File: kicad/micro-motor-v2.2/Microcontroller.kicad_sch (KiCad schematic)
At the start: 20 parts, among them J301 USB, J302 UART, J303 SWD, U301 STM32G474CET6

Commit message: ready to order
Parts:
- R305, R306: now not fitted; now left out of the parts list
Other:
- title: Micro-Motor V2.1 -> Micro-Motor V2.2
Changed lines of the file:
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@@
   (paper "A3")
   (title_block
-    (title "Micro-Motor V2.1")
+    (title "Micro-Motor V2.2")
     (date "2021-07-31")
     (rev "1")
@@
   (symbol (lib_id "stm32:STM32G474C(B-C-E)Tx_u") (at 228.6 127 180) (unit 2)
     (in_bom yes) (on_board yes) (dnp no)
-    (property "Reference" "U301" (at 227.1268 117.9322 0)
-      (effects (font (size 1.27 1.27)))
-    )
-    (property "Value" "STM32G474CET6" (at 227.1268 120.2436 0)
-      (effects (font (size 1.27 1.27)))
-    )
-    (property "Footprint" "LQFP48" (at 227.1268 122.555 0)
+    (property "Reference" "U301" (at 227.33 102.87 0)
+      (effects (font (size 1.27 1.27)))
+    )
+    (property "Value" "STM32G474CET6" (at 227.33 105.41 0)
+      (effects (font (size 1.27 1.27)))
+    )
+    (property "Footprint" "LQFP48" (at 227.33 151.13 0)
       (effects (font (size 1.27 1.27) italic))
     )
@@
   (symbol (lib_id "stm32:STM32G474C(B-C-E)Tx_u") (at 246.38 58.42 180) (unit 1)
     (in_bom yes) (on_board yes) (dnp no)
-    (property "Reference" "U301" (at 246.1768 49.3522 0)
-      (effects (font (size 1.27 1.27)))
-    )
-    (property "Value" "STM32G474CET6" (at 246.1768 51.6636 0)
-      (effects (font (size 1.27 1.27)))
-    )
-    (property "Footprint" "Package_QFP:LQFP-48_7x7mm_P0.5mm" (at 246.1768 53.975 0)
+    (property "Reference" "U301" (at 246.38 33.02 0)
+      (effects (font (size 1.27 1.27)))
+    )
+    (property "Value" "STM32G474CET6" (at 246.38 35.56 0)
+      (effects (font (size 1.27 1.27)))
+    )
+    (property "Footprint" "Package_QFP:LQFP-48_7x7mm_P0.5mm" (at 246.38 83.82 0)
       (effects (font (size 1.27 1.27) italic))
     )
@@
       (effects (font (size 1.27 1.27)))
     )
-    (property "Value" "STM32G474CET6" (at 353.06 184.15 0)
+    (property "Value" "STM32G474CET6" (at 347.98 184.15 0)
       (effects (font (size 1.27 1.27)))
     )
@@
   (symbol (lib_id "stm32:STM32G474C(B-C-E)Tx_u") (at 340.36 170.18 180) (unit 6)
     (in_bom yes) (on_board yes) (dnp no)
-    (property "Reference" "U301" (at 346.202 169.1386 0)
+    (property "Reference" "U301" (at 354.33 168.91 0)
       (effects (font (size 1.27 1.27)) (justify right))
     )
-    (property "Value" "STM32G474CET6" (at 346.202 171.45 0)
+    (property "Value" "STM32G474CET6" (at 354.33 171.45 0)
       (effects (font (size 1.27 1.27)) (justify right))
     )
-    (property "Footprint" "Package_QFP:LQFP-48_7x7mm_P0.5mm" (at 346.202 173.7614 0)
+    (property "Footprint" "Package_QFP:LQFP-48_7x7mm_P0.5mm" (at 354.33 173.99 0)
       (effects (font (size 1.27 1.27) italic) (justify right))
     )
@@
       (effects (font (size 1.27 1.27)) (justify left))
     )
-    (property "Value" "1k" (at 221.488 238.633 0)
+    (property "Value" "1k" (at 219.71 238.76 90)
       (effects (font (size 1.27 1.27)) (justify left))
     )
@@
   )
   (symbol (lib_id "Device:R") (at 238.76 237.49 0) (unit 1)
-    (in_bom yes) (on_board yes) (dnp no)
+    (in_bom no) (on_board yes) (dnp yes)
     (property "Reference" "R305" (at 240.538 236.3216 0)
       (effects (font (size 1.27 1.27)) (justify left))
     )
-    (property "Value" "1k" (at 240.538 238.633 0)
+    (property "Value" "1k" (at 238.76 238.76 90)
       (effects (font (size 1.27 1.27)) (justify left))
     )
@@
   )
   (symbol (lib_id "Device:R") (at 256.54 237.49 0) (unit 1)
-    (in_bom yes) (on_board yes) (dnp no)
+    (in_bom no) (on_board yes) (dnp yes)
     (property "Reference" "R306" (at 258.318 236.3216 0)
       (effects (font (size 1.27 1.27)) (justify left))
     )
-    (property "Value" "1k" (at 258.318 238.633 0)
-      (effects (font (size 1.27 1.27)) (justify left))
-    )
+    (property "Value" "1k" (at 256.54 238.76 90)
+      (effects (font (size 1.27 1.27)) (justify left))
+    )

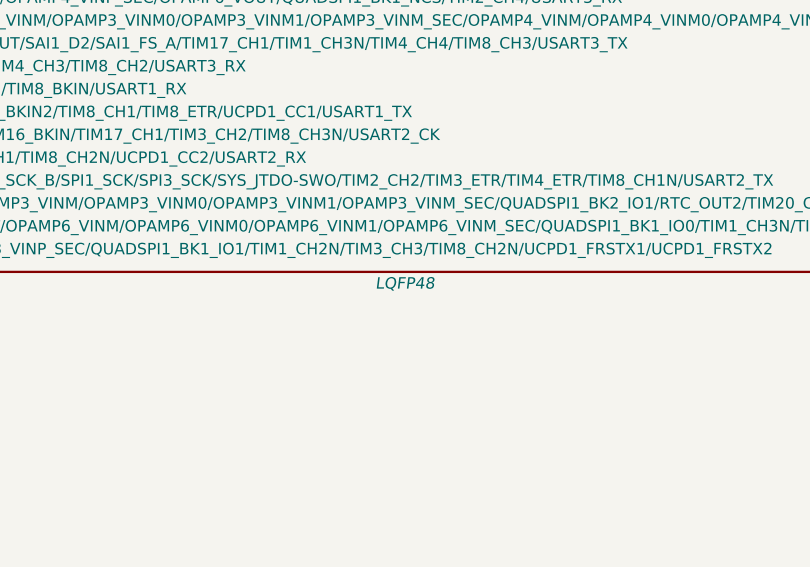
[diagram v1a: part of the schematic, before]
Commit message: [CI] Attempt to fix ERC
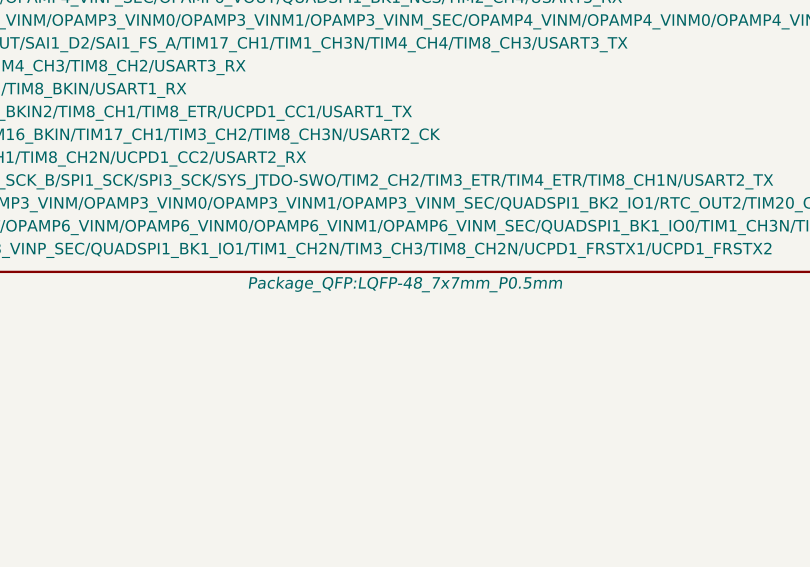
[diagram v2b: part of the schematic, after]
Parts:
- U301: footprint LQFP48 -> Package_QFP:LQFP-48_7x7mm_P0.5mm
